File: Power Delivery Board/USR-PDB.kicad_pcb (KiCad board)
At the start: 2 copper layers, 100 x 150 mm, 31 parts, among them U10 Anderson PP45 Vert. 2x1, U11 Anderson PP45 Vert. 2x1, U12 TL2575HV-05IKV, U13 MCP3002-I/P, U2 LM2676T-12_NOPB, U5 Anderson PP45 Vert. 2x1, U6 Anderson PP45 Vert. 2x1, U7 Anderson PP45 Vert. 2x1, U8 Anderson PP45 Vert. 2x1, U9 Anderson PP45 Vert. 2x1

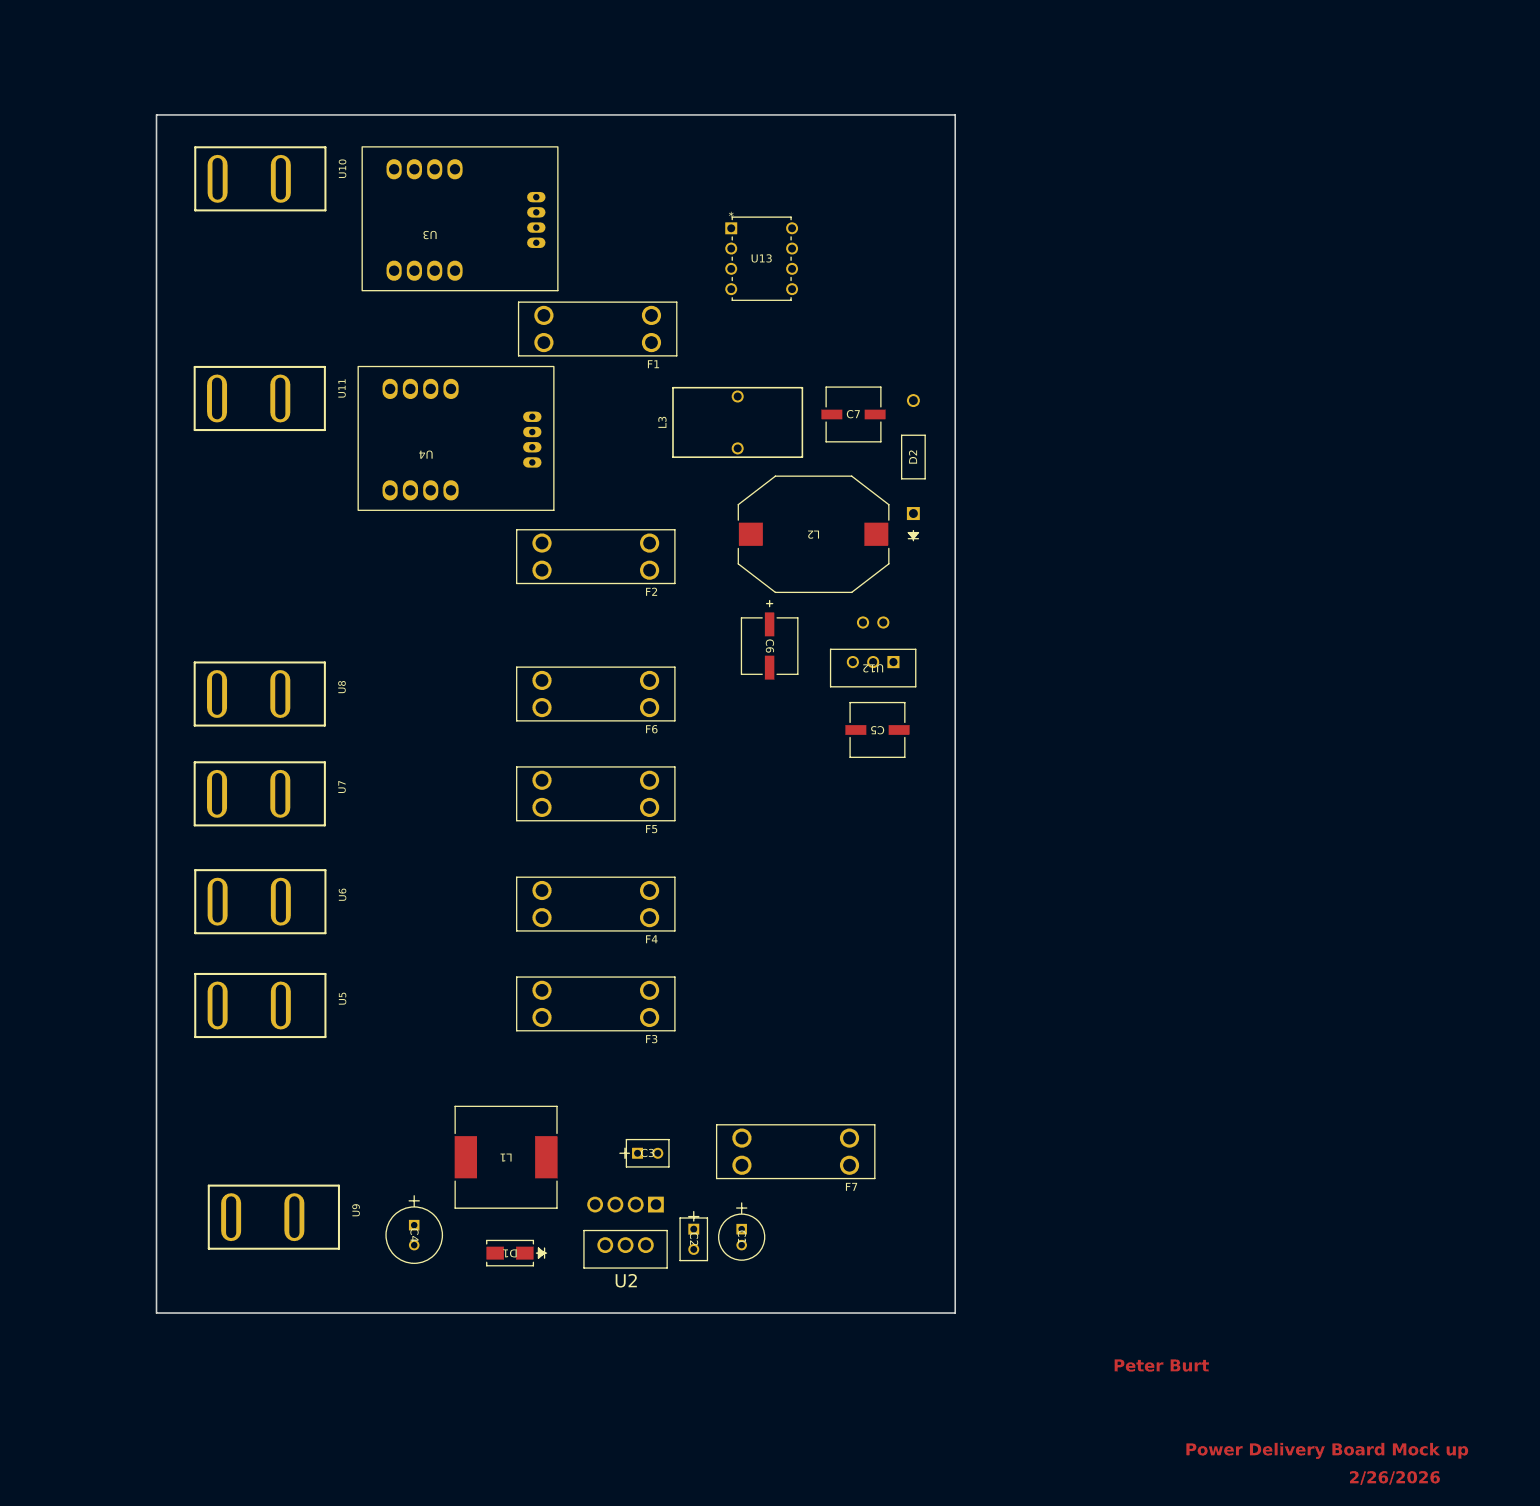
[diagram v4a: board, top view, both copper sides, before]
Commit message: traces added for the power delivery boards PCB
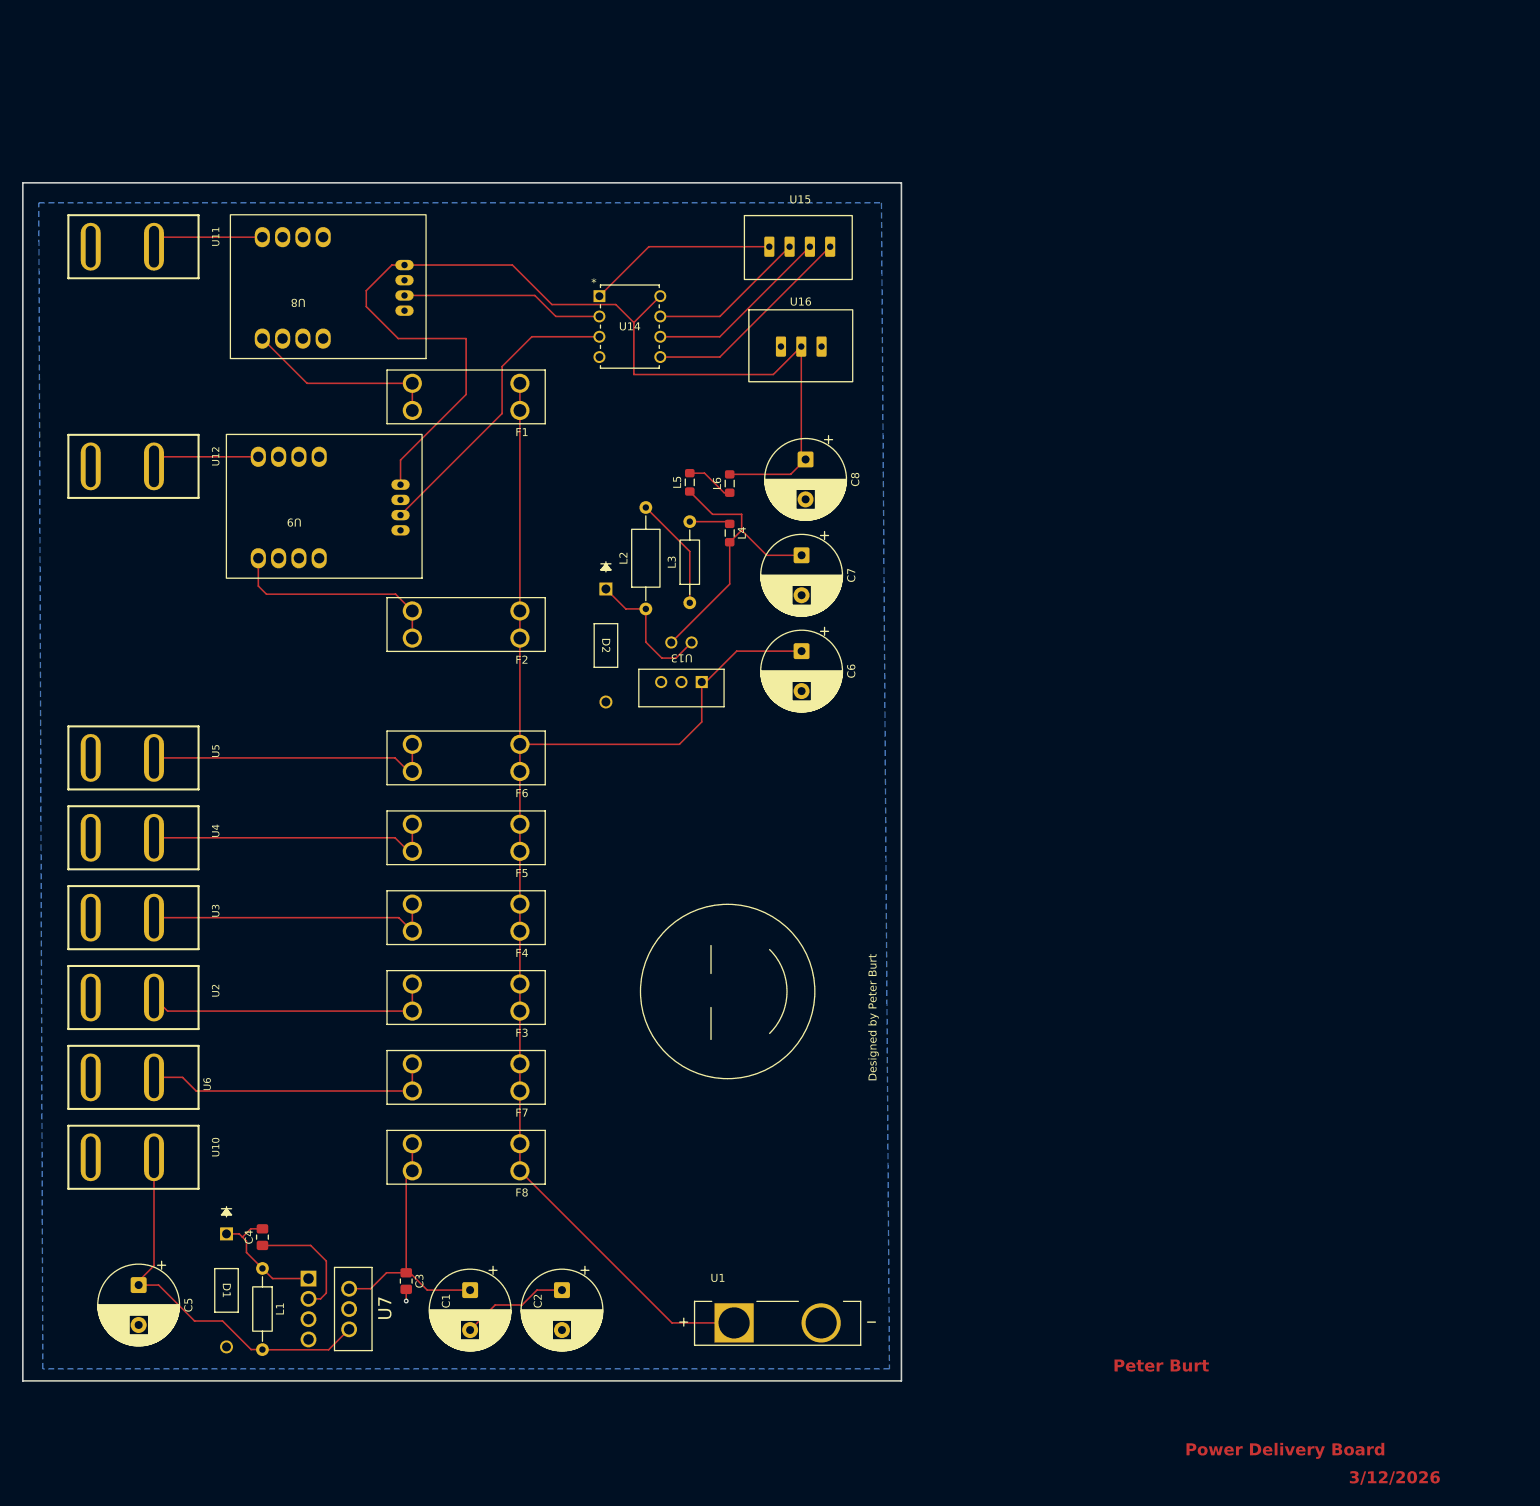
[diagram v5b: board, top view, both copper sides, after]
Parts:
- added C2: 100uF, Capacitor_THT:CP_Radial_D10.0mm_P5.00mm, F.Cu at (109.0, 169.6)
- added F7: Extra fuse holder, USR:FUSE_3557-15, F.Cu at (97.0, 143.0)
- added L3: 100uH, Inductor_THT:L_Axial_L5.3mm_D2.2mm_P10.16mm_Horizontal_Vishay_IM-1, F.Cu at (125.0, 83.6)
- added L4: 10uH, Inductor_SMD:L_0805_2012Metric_Pad1.05x1.20mm_HandSolder, F.Cu at (130.0, 74.8)
- added L6: 10uH, Inductor_SMD:L_0805_2012Metric_Pad1.05x1.20mm_HandSolder, F.Cu at (130.0, 68.7)
- added U1: XT90, USR:AMASS_XT90PW-M_VERTICAL, F.Cu at (136.0, 174.0)
- added U15: ~, USR:JST-XA 4-PIN, F.Cu at (138.8, 33.6)
- added U16: ~, USR:JST-XA 3-PIN, F.Cu at (138.9, 46.4)
- added U6: Anderson PP45 Vert. 2x1, USR:ANDERSON PP45 VERT. 2X1, F.Cu at (50.0, 143.0)
- C1: value 56uF -> 100uF; footprint USR:CAP_WCAP-ATUL_05.0X11.0_WRE -> Capacitor_THT:CP_Radial_D10.0mm_P5.00mm
- C3: renamed from C2; footprint USR:CAP_C320C_MOLDED RADIAL_KEM -> Capacitor_SMD:C_0805_2012Metric_Pad1.18x1.45mm_HandSolder
- C4: renamed from C3; footprint USR:CAP_C320C_MOLDED RADIAL_KEM -> Capacitor_SMD:C_0805_2012Metric_Pad1.18x1.45mm_HandSolder
- C5: renamed from C4; value 82uF -> 100uF; footprint USR:CAP_ATLL_06p3X15p0_WRE -> Capacitor_THT:CP_Radial_D10.0mm_P5.00mm
- C6: renamed from C5; footprint USR:U2-K_NCH -> Capacitor_THT:CP_Radial_D10.0mm_P5.00mm
- C7: renamed from C6; footprint USR:PCAP_6.3x7.7-ELECT_NCA -> Capacitor_THT:CP_Radial_D10.0mm_P5.00mm
- C8: renamed from C7; footprint USR:U2-K_NCH -> Capacitor_THT:CP_Radial_D10.0mm_P5.00mm
- D1: value 700mV 2A -> 1N5821; footprint USR:SMA_DIO -> USR:DO-41_STM
- L1: footprint USR:IND_BOURNS_SRR1210 -> Inductor_THT:L_Axial_L5.3mm_D2.2mm_P10.16mm_Horizontal_Vishay_IM-1
- L2: value 330uH -> 220uH; footprint USR:IND_BOURNS_SDR1806 -> Inductor_THT:L_Axial_L7.0mm_D3.3mm_P12.70mm_Horizontal_Fastron_MICC
- L5: renamed from L3; value 20uH -> 10uH; footprint USR:WE-FI_7447025 -> Inductor_SMD:L_0805_2012Metric_Pad1.05x1.20mm_HandSolder
- moved C4 48.1 mm to (71.5, 163.0), turned to 90 degrees
- moved F8 41.3 mm to (97.0, 153.0)
- moved D2 39.6 mm to (114.5, 81.9), turned to -90 degrees
- moved C3 36.6 mm to (89.5, 168.5)
- moved D1 35.6 mm to (67.0, 162.6), turned to -90 degrees
- moved C5 35.3 mm to (56.0, 169.0)
- moved C1 34.8 mm to (97.5, 169.6)
- moved L1 33.5 mm to (71.5, 166.9), turned to -90 degrees
- moved U7 25.3 mm to (88.5, 175.8), turned to -90 degrees
- moved U13 24.1 mm to (121.4, 95.0)
- moved L2 23.0 mm to (119.5, 84.3), turned to 90 degrees
- moved U10 19.1 mm to (50.0, 153.0)
- moved U14 18.6 mm to (113.7, 45.2)
- moved U8 18.6 mm to (76.0, 45.0)
- moved U9 18.6 mm to (75.5, 72.5)
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- renumbered F7 to F8, U9 to U10, U10 to U11, U11 to U12, U12 to U13, U13 to U14, U5 to U2, U6 to U3, U7 to U4, U8 to U5, U2 to U7, U3 to U8, U4 to U9
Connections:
- C1 pad 2: GND -> Net-(C1-Pad2)
- C7 pad 1: Net-(U12-FEEDBACK) -> Net-(U13-FEEDBACK)
- L2 pad 2: Net-(U12-FEEDBACK) -> Net-(L2-Pad2)
- L5 pad 1: Net-(U12-FEEDBACK) -> Net-(U13-FEEDBACK)
- L5 pad 2: 5V -> Net-(L5-Pad2)
- U13 pad 4: Net-(U12-FEEDBACK) -> Net-(U13-FEEDBACK)
- U14 pad 1: unconnected-(U13-CS/SHDN-Pad1) -> CS
- U14 pad 5: unconnected-(U13-Din-Pad5) -> Din
- U14 pad 6: unconnected-(U13-Dout-Pad6) -> Dout
- U14 pad 7: unconnected-(U13-CLK-Pad7) -> CLK
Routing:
- net Vin: track 0.00 -> 176.3 mm
- net 5V: track 0.00 -> 133.9 mm
- net Net-(U10-VCC): track 0.00 -> 47.6 mm
- net HE2_out: track 0.00 -> 37.6 mm
- net Net-(U5-VCC): track 0.00 -> 36.4 mm
- net Net-(U4-VCC): track 0.00 -> 36.4 mm
- net Net-(U3-VCC): track 0.00 -> 36.4 mm
- net Net-(U6-VCC): track 0.00 -> 36.4 mm
- net Net-(U2-VCC): track 0.00 -> 36.4 mm
- net Net-(U13-FEEDBACK): track 0.00 -> 36.2 mm
- net Net-(U7-VIN): track 0.00 -> 33.4 mm
- net HE_sensor2: track 0.00 -> 27.5 mm
- net Din: track 0.00 -> 27.0 mm
- net HE1_out: track 0.00 -> 25.5 mm
- net HE_sensor1: track 0.00 -> 24.5 mm
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- added copper zone on B.Cu, net GND
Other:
- board size 100 x 150 mm -> 110 x 150 mm
- board text added: "3/12/2026"
- board text added: "Designed by Peter Burt"
- board text added: "Power Delivery Board"
- board text removed: "2/26/2026"
- board text removed: "Power Delivery Board Mock up"

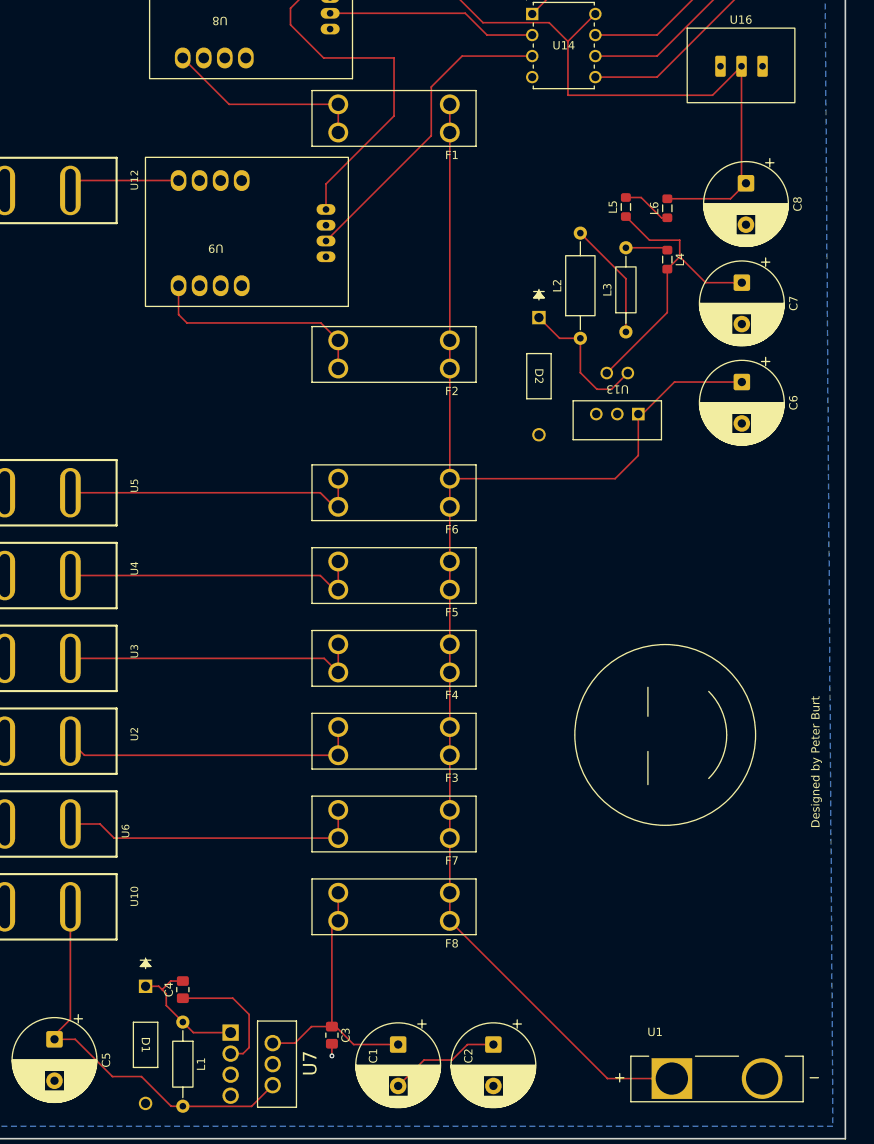
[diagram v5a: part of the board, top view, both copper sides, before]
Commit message: updated trace sizes for PDB
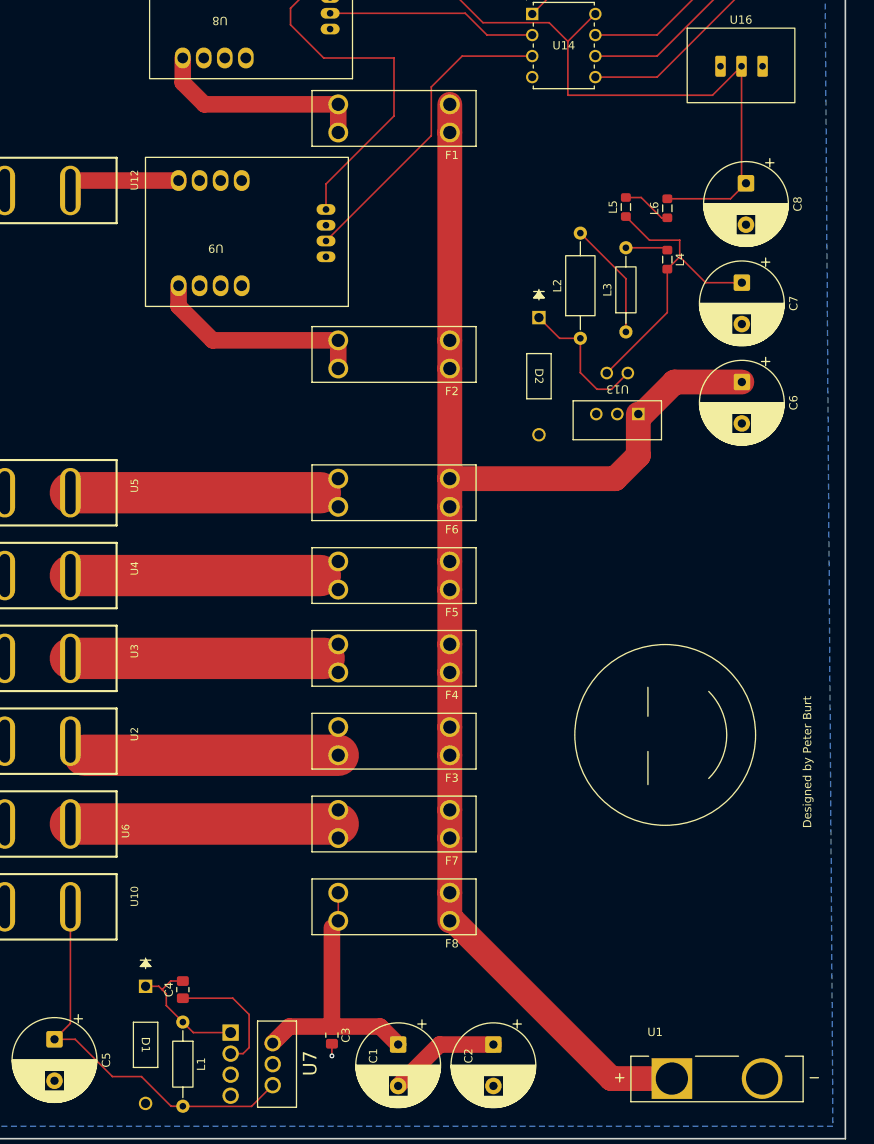
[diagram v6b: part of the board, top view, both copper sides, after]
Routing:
- net Net-(U7-VIN): track 33.4 -> 37.2 mm
- net HE_sensor1: track 24.5 -> 26.2 mm
- net Net-(U6-VCC): track 36.4 -> 35.7 mm
- net HE_sensor2: track 27.5 -> 26.9 mm
